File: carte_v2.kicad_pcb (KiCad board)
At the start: 2 copper layers, 81.3 x 68.6 mm, 22 parts, among them J1 Conn_01x03_Socket, J2 Conn_01x04_Socket, J3 Conn_01x03_Socket, J4 Conn_01x03_Socket, J5 Conn_01x04_Socket, J6 Conn_01x03_Socket, J7 Conn_02x20_Odd_Even, J8 Conn_01x04_Socket, J9 Conn_01x04_Socket, SW1 SW_Push_Dual, SW2 SW_Push_Dual, SW3 SW_Push_Dual, U1 Arduino_Nano

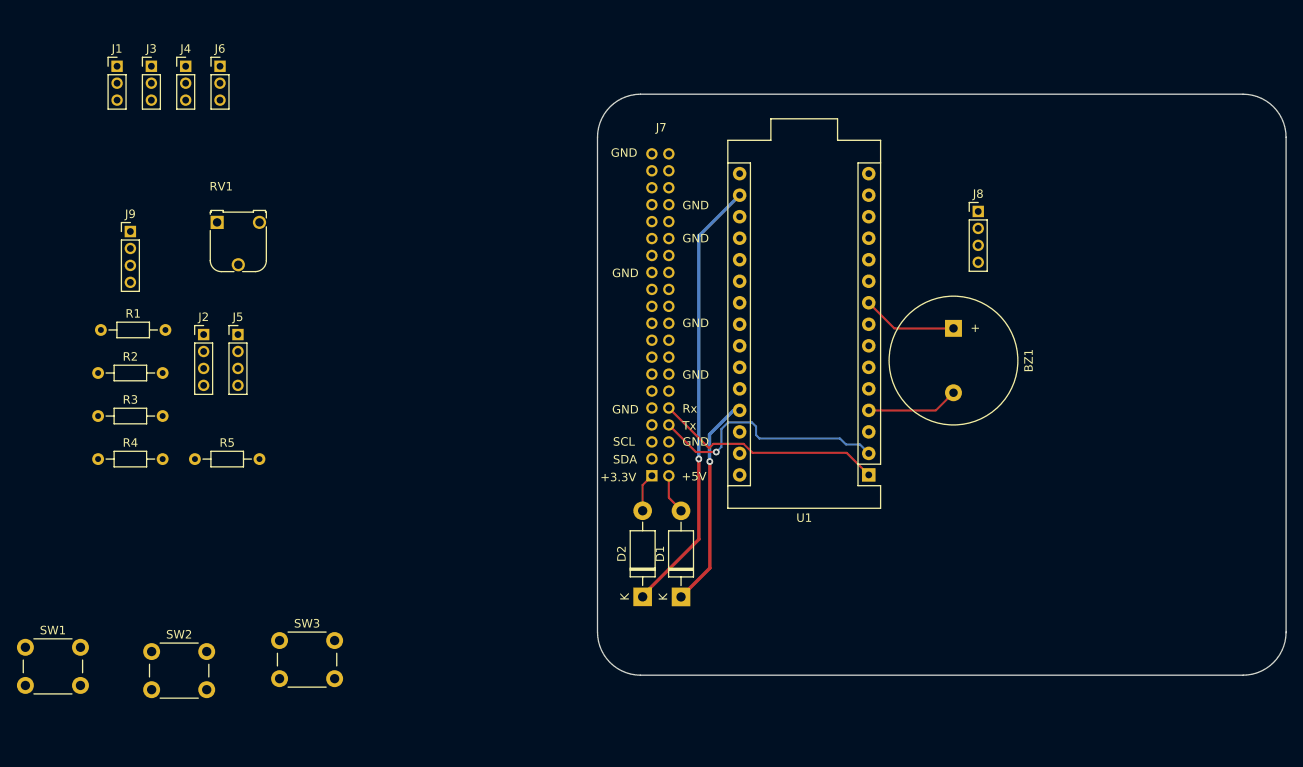
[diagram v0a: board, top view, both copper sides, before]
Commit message: almost finished routing (missing buttons)
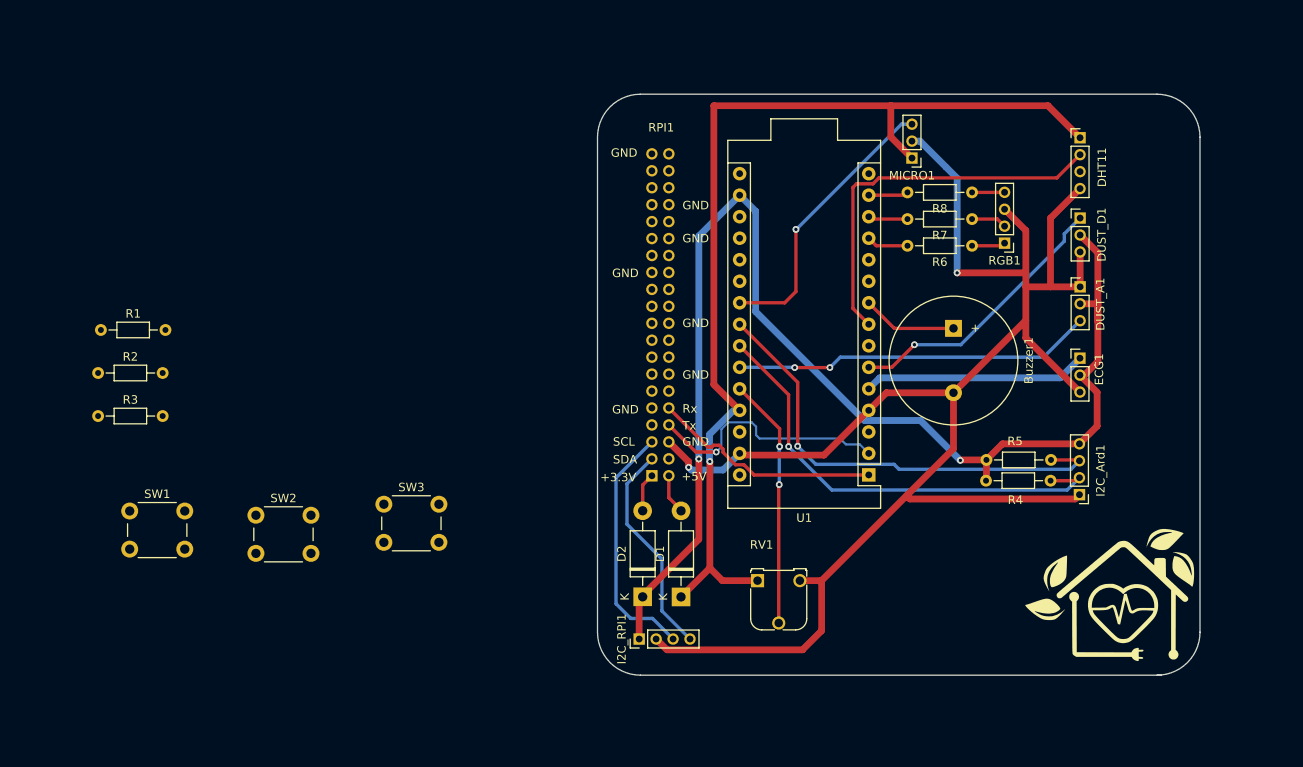
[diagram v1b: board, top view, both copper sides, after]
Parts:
- added G***: LOGO, LOGO, F.Cu at (179.8, 98.0)
- added R6: 220, Resistor_THT:R_Axial_DIN0204_L3.6mm_D1.6mm_P7.62mm_Horizontal, F.Cu at (163.6, 53.5)
- added R7: 220, Resistor_THT:R_Axial_DIN0204_L3.6mm_D1.6mm_P7.62mm_Horizontal, F.Cu at (163.6, 50.3)
- added R8: 220, Resistor_THT:R_Axial_DIN0204_L3.6mm_D1.6mm_P7.62mm_Horizontal, F.Cu at (163.6, 47.1)
- moved DUST_A1 112.7 mm to (176.3, 58.3)
- moved R4 112.5 mm to (172.9, 81.2), turned to 180 degrees
- moved ECG1 107.2 mm to (176.3, 66.7)
- moved DUST_D1 107.1 mm to (176.3, 50.2)
- moved DHT11 106.0 mm to (176.3, 40.7)
- moved I2C_Ard1 101.1 mm to (176.3, 82.8), turned to 180 degrees
- moved R5 101.1 mm to (172.9, 78.7), turned to 180 degrees
- moved MICRO1 94.5 mm to (156.5, 43.1), turned to 180 degrees
- moved I2C_RPI1 76.9 mm to (124.3, 99.9), turned to 90 degrees
- moved RV1 76.5 mm to (138.3, 93.0)
- moved SW3 20.3 mm to (94.2, 84.0)
- moved SW2 20.3 mm to (79.1, 85.3)
- moved SW1 20.3 mm to (64.2, 84.8)
- moved RGB1 4.86 mm to (167.4, 53.1), turned to 180 degrees
- renumbered BZ1 to Buzzer1, J2 to DHT11, J3 to DUST_A1, J4 to DUST_D1, J6 to ECG1, J5 to I2C_Ard1, J9 to I2C_RPI1, J1 to MICRO1, J8 to RGB1, J7 to RPI1
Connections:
- RGB1 pad 1: /BLUE -> Net-(RGB1-Pin_1)
- RGB1 pad 2: /GREEN -> Net-(RGB1-Pin_2)
- RGB1 pad 4: /RED -> Net-(RGB1-Pin_4)
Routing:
- net GND: track 10.9 -> 206.5 mm, vias 0 -> 2
- net +3.3V: track 52.4 -> 153.4 mm, vias 1 -> 2
- net +5V: track 26.4 -> 121.9 mm
- net /SDA_CO2: track 0.00 -> 55.6 mm, vias 0 -> 1
- net /SCL_CO2: track 0.00 -> 54.9 mm, vias 0 -> 1
- net /DHT11: track 0.00 -> 45.3 mm
- net /SHARP_ANALOG: track 0.00 -> 42.5 mm, vias 0 -> 2
- net /MICROPHONE: track 0.00 -> 33.4 mm, vias 0 -> 1
- net /SHARP_DIGITAL: track 0.00 -> 32.8 mm, vias 0 -> 1
- net /POT: track 0.00 -> 29.6 mm, vias 0 -> 2
- net /SCL_OLED: track 0.00 -> 29.3 mm
- net /ECG: track 0.00 -> 26.4 mm
- net /SDA_OLED: track 0.00 -> 25.6 mm
- net /BLUE: track 0.00 -> 4.94 mm
- net /RED: track 0.00 -> 4.89 mm
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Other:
- board size 81.3 x 68.6 mm -> 71.1 x 68.6 mm

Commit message: routing finished, need to resolve error
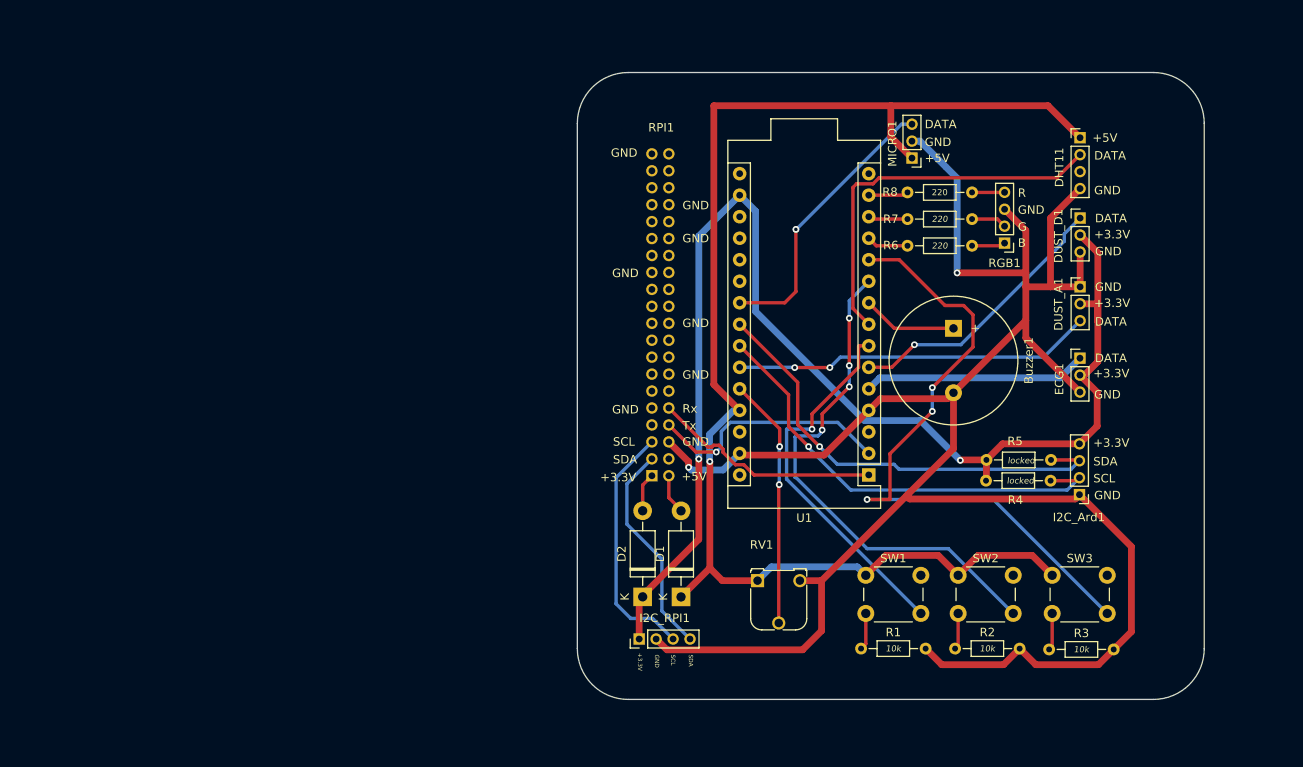
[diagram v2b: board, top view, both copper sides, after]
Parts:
- removed G***: LOGO, LOGO
- SW1, SW2, SW3: footprint Button_Switch_THT:SW_PUSH_6mm_H5mm -> Button_Switch_THT:SW_PUSH_6mm_H5mm_PATCHED
- moved R3 115.6 mm to (172.7, 101.1)
- moved R2 106.3 mm to (161.6, 101.0)
- moved R1 97.3 mm to (150.5, 101.0)
- moved SW1 87.2 mm to (151.1, 92.3)
- moved SW2 83.2 mm to (161.9, 92.3)
- moved SW3 79.3 mm to (173.1, 92.3)
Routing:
- net /SW3: track 0.00 -> 77.5 mm, vias 0 -> 3
- net /SW2: track 0.00 -> 60.7 mm, vias 0 -> 4
- net GND: track 206.5 -> 253.5 mm
- net /SW1: track 0.00 -> 44.6 mm, vias 0 -> 1
- net +5V: track 121.9 -> 161.6 mm
- net Net-(R3-Pad1): track 0.00 -> 4.40 mm
- net Net-(R1-Pad1): track 0.00 -> 4.38 mm
- net Net-(R2-Pad1): track 0.00 -> 4.30 mm
- net /SDA_CO2: track 55.6 -> 54.1 mm
- net /SCL_CO2: track 54.9 -> 53.6 mm
- net /Tx_RPI: track 29.7 -> 29.0 mm
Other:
- board size 71.1 x 68.6 mm -> 74 x 74 mm
- board text added: "B"
- board text added: "DATA"
- board text added: "G"
- board text added: "R"

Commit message: added mouting hole + routing over with no error
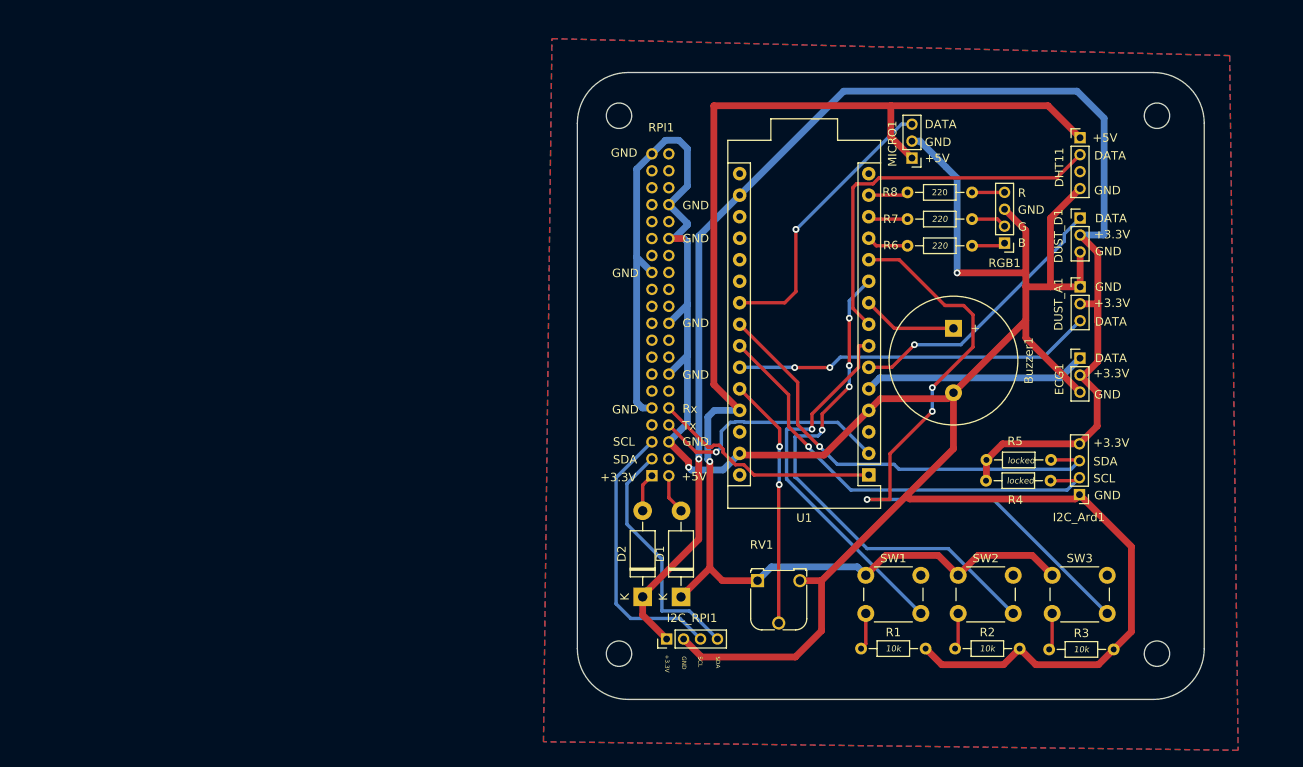
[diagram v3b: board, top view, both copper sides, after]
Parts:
- added H1: MountingHole, MountingHole:MountingHole_3mm, F.Cu at (185.4, 38.1)
- added H2: MountingHole, MountingHole:MountingHole_3mm, F.Cu at (121.9, 38.1)
- added H3: MountingHole, MountingHole:MountingHole_3mm, F.Cu at (185.4, 101.6)
- added H4: MountingHole, MountingHole:MountingHole_3mm, F.Cu at (121.9, 101.6)
- moved I2C_RPI1 3.24 mm to (127.5, 99.9)
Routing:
- net GND: track 253.5 -> 339.7 mm
- net +3.3V: track 153.4 -> 171.9 mm, vias 2 -> 1
- net /SCL_OLED: track 29.3 -> 32.6 mm
- net /SDA_OLED: track 25.6 -> 28.8 mm
- net +5V: track 161.6 -> 163.1 mm
- added copper zone on B.Cu, net GND
- added copper zone on F.Cu, net GND

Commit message: created fabrications files
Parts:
- added G***: LOGO, LOGO, F.Cu at (158.4, 81.7)
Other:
- board text added: "ECO-FRIENDLY HEALTH MONITORING"
- board text added: "TAKE EIR"
- board text added: "health-eir v2 - version 1.0 - Made by Theophile Wemaere - May 2023"

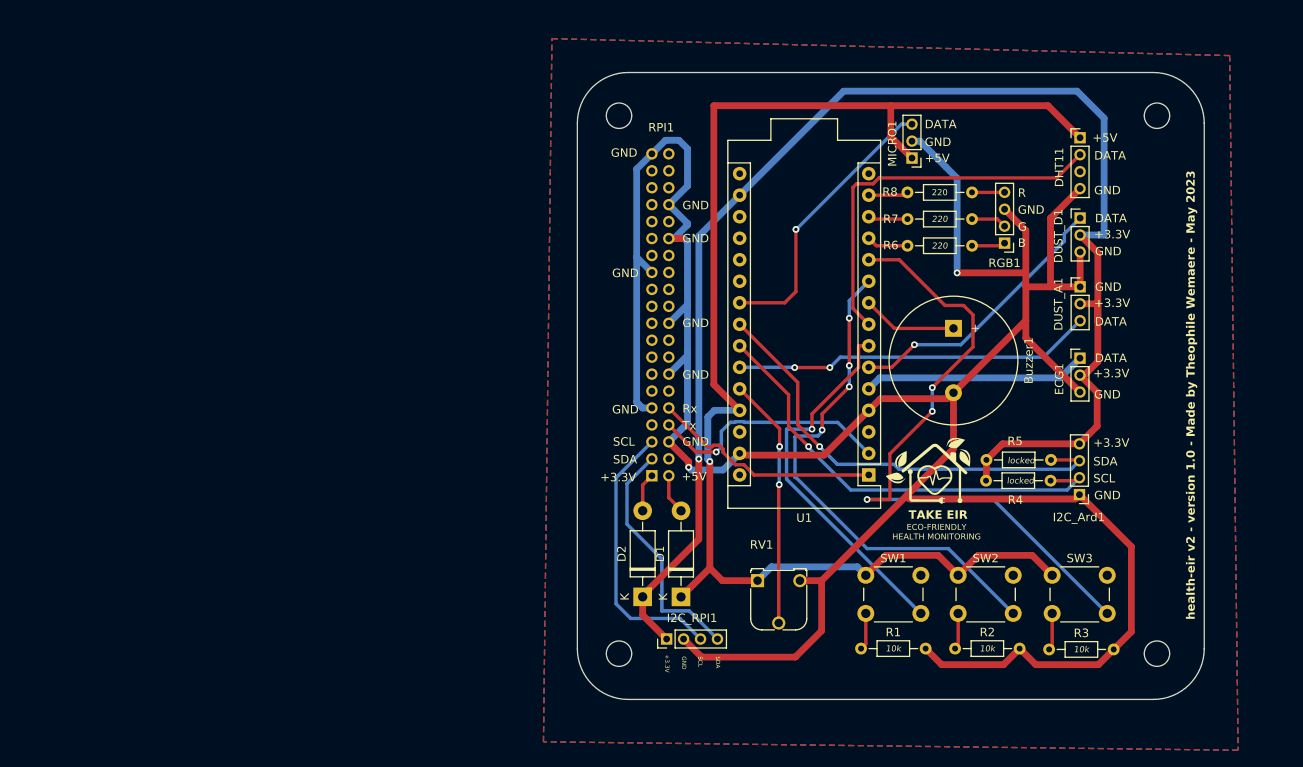
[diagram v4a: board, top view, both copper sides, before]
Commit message: remake rpi footprint
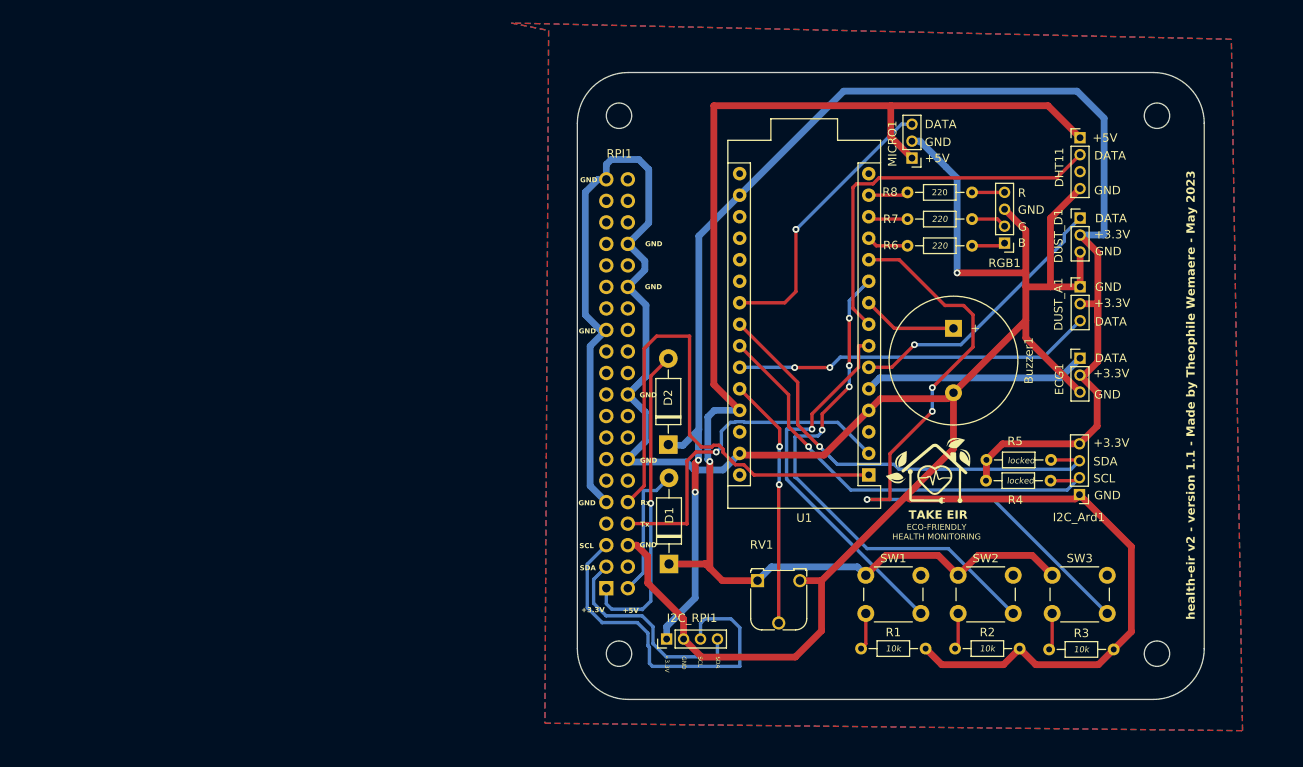
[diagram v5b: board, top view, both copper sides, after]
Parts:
- RPI1: footprint Connector_PinHeader_2.00mm:PinHeader_2x20_P2.00mm_Vertical -> Connector_PinHeader_2.54mm:PinHeader_2x20_P2.54mm_Vertical
- moved D2 18.2 mm to (127.7, 76.9)
- moved RPI1 14.3 mm to (120.4, 93.9)
- moved D1 4.14 mm to (127.8, 91.0)
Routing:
- net /Rx_RPI: track 27.3 -> 60.1 mm
- net Net-(D2-A): track 4.58 -> 37.3 mm, vias 0 -> 1
- net GND: track 339.7 -> 359.6 mm, vias 2 -> 1
- net /Tx_RPI: track 29.0 -> 40.4 mm
- net Net-(D1-A): track 4.81 -> 15.9 mm
- net /SCL_OLED: track 32.6 -> 42.9 mm
- net /SDA_OLED: track 28.8 -> 25.4 mm
- net +3.3V: track 171.9 -> 172.9 mm, vias 1 -> 2
- net +5V: track 163.1 -> 162.3 mm
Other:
- board text added: "health-eir v2 - version 1.1 - Made by Theophile Wemaere - May 2023"
- board text removed: "health-eir v2 - version 1.0 - Made by Theophile Wemaere - May 2023"

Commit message: added 3D models
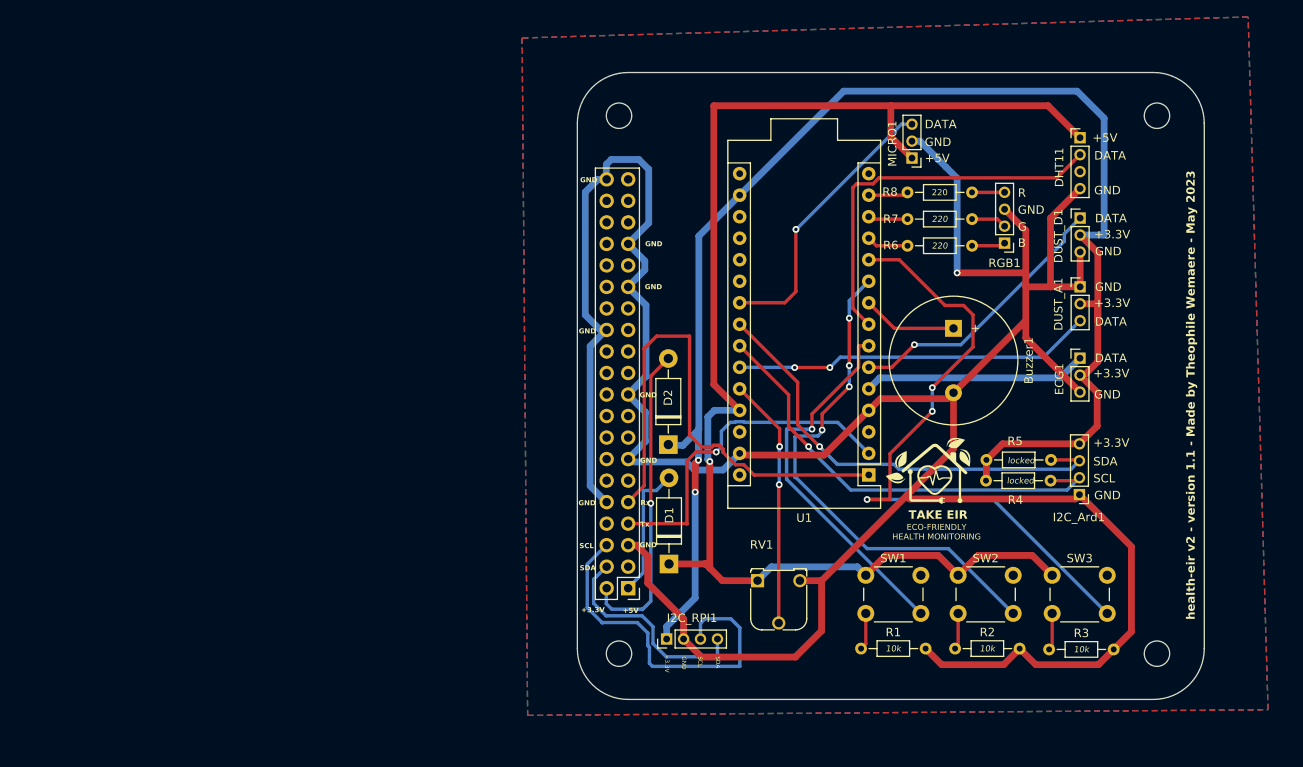
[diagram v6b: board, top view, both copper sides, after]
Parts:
- RPI1: moved to F.Cu
- moved RPI1 2.58 mm to (123.0, 93.9), turned to 180 degrees
